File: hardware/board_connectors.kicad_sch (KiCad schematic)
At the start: 15 parts, among them J1 AudioJack2_Ground, J3 Conn_01x02, J5 AudioJack2_Ground, J6 Conn_02x03_Odd_Even, J7 AudioJack2_Ground, J7 USB_B_Micro

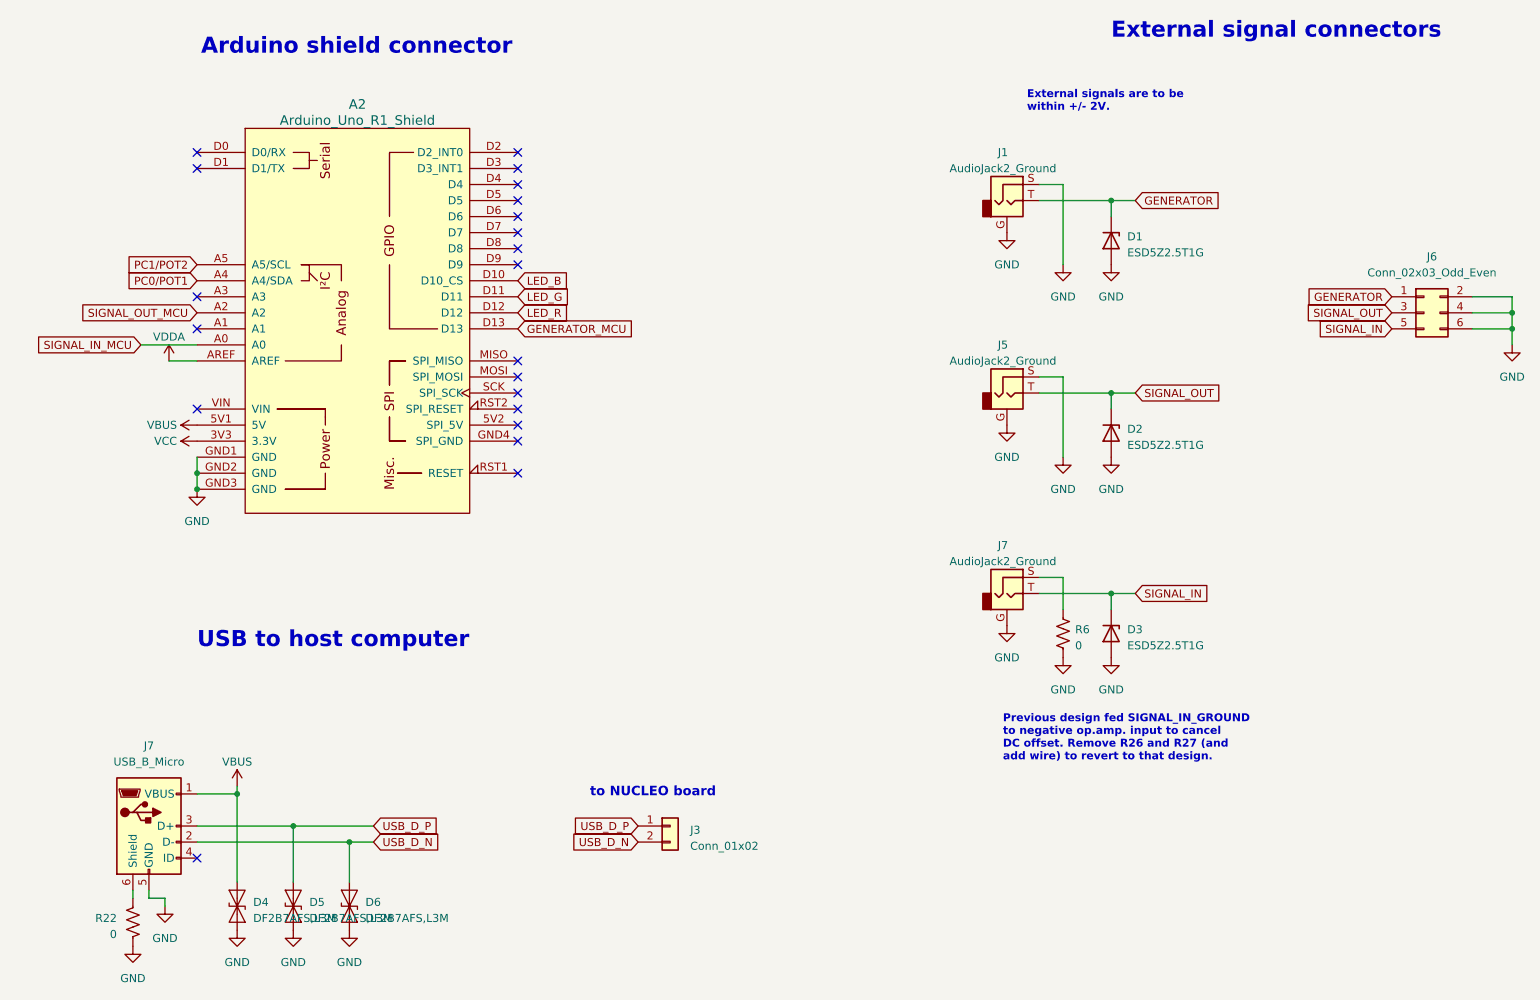
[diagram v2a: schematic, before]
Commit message: use nucleo 3.3v vdda; add 2nd low-pass stage to input
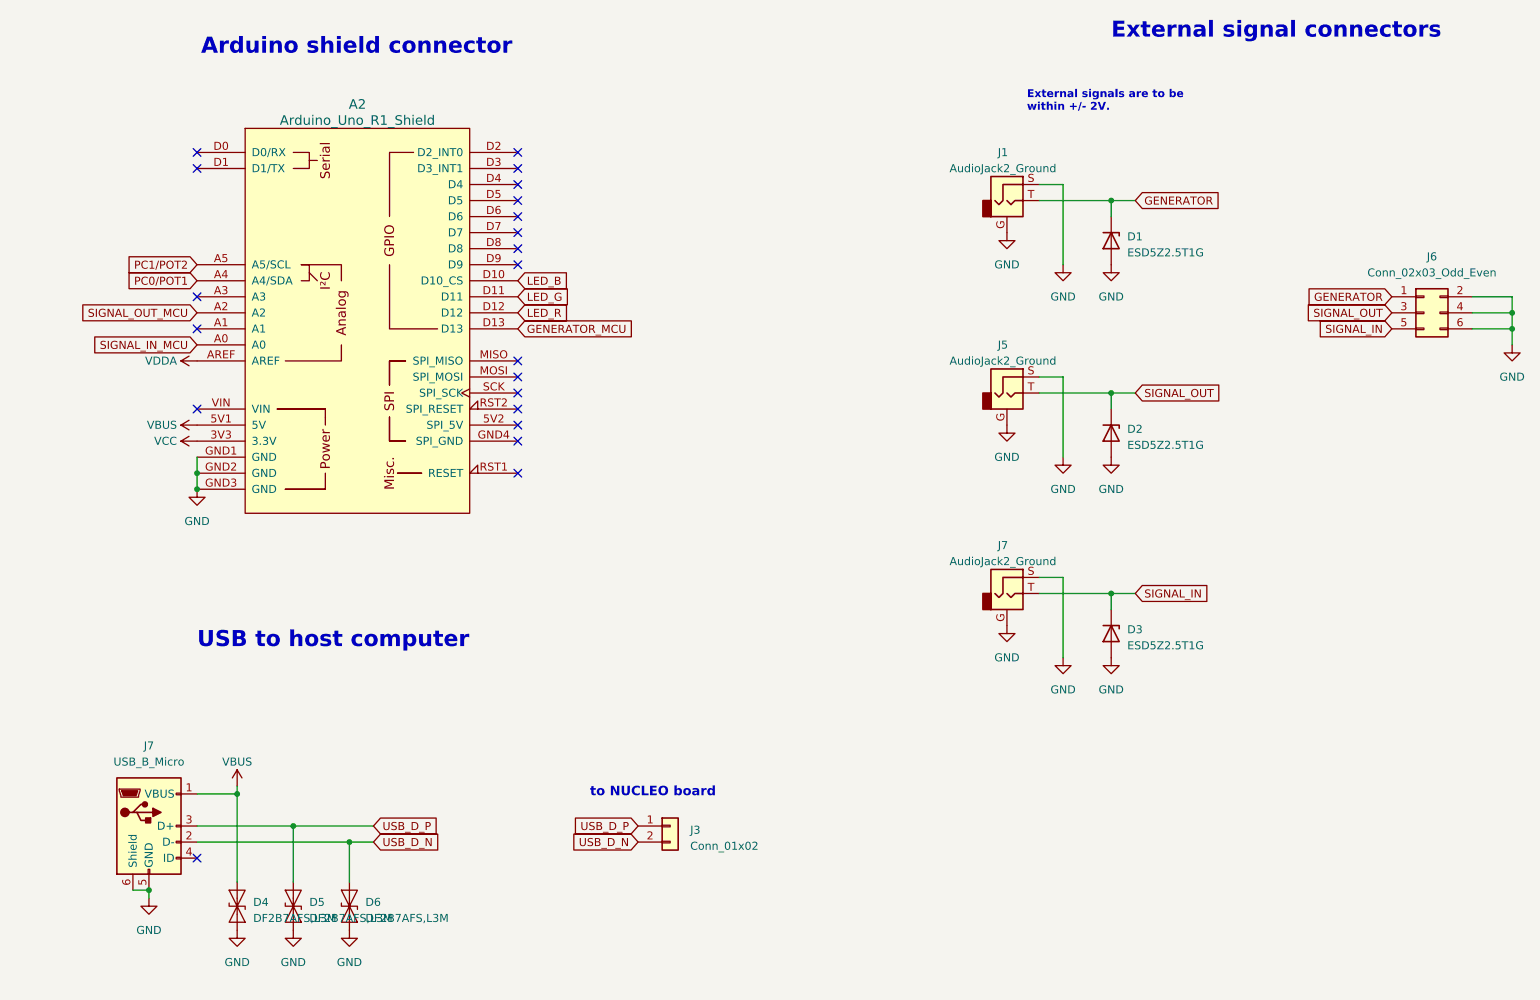
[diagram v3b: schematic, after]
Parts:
- removed R22, R6: 0, Resistor_SMD:R_0603_1608Metric, symbol Device:R_US
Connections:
- net GND: now also J7.6 (Shield), J7.S
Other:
- note removed: "Previous design fed SIGNAL_IN_GROUND to negative op.amp. input to cancel DC offset. Remove R26 and R27 (and add wire) to revert to that design."
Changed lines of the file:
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@@
   (title_block
     (title "DSP PAW add-on board")
-    (date "2023-09-04")
+    (date "2023-09-13")
     (rev "2")
     (company "bitgloo")
@@
   )
   (junction (at 257.81 72.39) (diameter 0) (color 0 0 0 0)
+  )
+  (junction (at 41.91 163.83) (diameter 0) (color 0 0 0 0)
   )
   (junction (at 49.53 97.79) (diameter 0) (color 0 0 0 0)
@@
     (stroke (width 0) (type default))
   )
-  (wire (pts (xy 186.69 114.3) (xy 186.69 119.38))
+  (wire (pts (xy 186.69 114.3) (xy 186.69 127))
     (stroke (width 0) (type default))
   )
@@
     (stroke (width 0) (type default))
   )
-  (wire (pts (xy 45.085 80.01) (xy 49.53 80.01))
-    (stroke (width 0) (type default))
-  )
   (wire (pts (xy 194.31 54.61) (xy 194.31 57.15))
     (stroke (width 0) (type default))
@@
     (stroke (width 0) (type default))
   )
+  (wire (pts (xy 39.37 163.83) (xy 41.91 163.83))
+    (stroke (width 0) (type default))
+  )
   (wire (pts (xy 194.31 85.09) (xy 194.31 87.63))
     (stroke (width 0) (type default))
@@
     (stroke (width 0) (type default))
   )
-  (wire (pts (xy 40.64 77.47) (xy 49.53 77.47))
-    (stroke (width 0) (type default))
-  )
-  (wire (pts (xy 44.45 165.1) (xy 41.91 165.1))
-    (stroke (width 0) (type default))
-  )
   (wire (pts (xy 182.88 52.07) (xy 186.69 52.07))
     (stroke (width 0) (type default))
@@
     (stroke (width 0) (type default))
   )
-  (wire (pts (xy 39.37 163.83) (xy 39.37 165.1))
-    (stroke (width 0) (type default))
-  )
   (wire (pts (xy 49.53 95.25) (xy 49.53 97.79))
     (stroke (width 0) (type default))
@@
     (stroke (width 0) (type default))
   )
-  (wire (pts (xy 44.45 166.37) (xy 44.45 165.1))
-    (stroke (width 0) (type default))
-  )
-  (wire (pts (xy 41.91 165.1) (xy 41.91 163.83))
-    (stroke (width 0) (type default))
-  )
   (wire (pts (xy 64.77 153.67) (xy 64.77 162.56))
+    (stroke (width 0) (type default))
+  )
+  (wire (pts (xy 41.91 163.83) (xy 41.91 165.1))
     (stroke (width 0) (type default))
   )
@@
   (text "External signal connectors" (at 194.31 29.21 0)
     (effects (font (size 2.54 2.54) (thickness 0.254) bold) (justify left bottom))
-  )
-  (text "Previous design fed SIGNAL_IN_GROUND\nto negative op.amp. input to cancel\nDC offset. Remove R26 and R27 (and\nadd wire) to revert to that design."
-    (at 177.165 143.51 0)
-    (effects (font (size 1.25 1.25) (thickness 0.254) bold) (justify left bottom))
   )
   (global_label "USB_D_P" (shape input) (at 119.38 153.67 180) (fields_autoplaced)
@@
     )
   )
-  (global_label "SIGNAL_IN_MCU" (shape input) (at 40.64 77.47 180) (fields_autoplaced)
+  (global_label "SIGNAL_IN_MCU" (shape input) (at 49.53 77.47 180) (fields_autoplaced)
     (effects (font (size 1.27 1.27)) (justify right))
-    (property "Intersheetrefs" "${INTERSHEET_REFS}" (at 23.2803 77.47 0)
+    (property "Intersheetrefs" "${INTERSHEET_REFS}" (at 32.1703 77.47 0)
       (effects (font (size 1.27 1.27)) (justify right) hide)
     )
@@
     )
   )
-  (symbol (lib_id "power:VDDA") (at 45.085 80.01 0) (unit 1)
+  (symbol (lib_id "power:VDDA") (at 49.53 80.01 90) (unit 1)
     (in_bom yes) (on_board yes) (dnp no)
-    (property "Reference" "#PWR04" (at 45.085 83.82 0)
-      (effects (font (size 1.27 1.27)) hide)
-    )
-    (property "Value" "VDDA" (at 45.085 76.2 0)
-      (effects (font (size 1.27 1.27)))
-    )
-    (property "Footprint" "" (at 45.085 80.01 0)
-      (effects (font (size 1.27 1.27)) hide)
-    )
-    (property "Datasheet" "" (at 45.085 80.01 0)
+    (property "Reference" "#PWR04" (at 53.34 80.01 0)
+      (effects (font (size 1.27 1.27)) hide)
+    )
+    (property "Value" "VDDA" (at 46.355 80.01 90)
+      (effects (font (size 1.27 1.27)) (justify left))
+    )
+    (property "Footprint" "" (at 49.53 80.01 0)
+      (effects (font (size 1.27 1.27)) hide)
+    )
+    (property "Datasheet" "" (at 49.53 80.01 0)
       (effects (font (size 1.27 1.27)) hide)
     )
@@
     )
   )
-  (symbol (lib_id "power:GND") (at 44.45 166.37 0) (unit 1)
-    (in_bom yes) (on_board yes) (dnp no) (fields_autoplaced)
-    (property "Reference" "#PWR038" (at 44.45 172.72 0)
-      (effects (font (size 1.27 1.27)) hide)
-    )
-    (property "Value" "GND" (at 44.45 171.45 0)
-      (effects (font (size 1.27 1.27)))
-    )
-    (property "Footprint" "" (at 44.45 166.37 0)
-      (effects (font (size 1.27 1.27)) hide)
-    )
-    (property "Datasheet" "" (at 44.45 166.37 0)
-      (effects (font (size 1.27 1.27)) hide)
-    )
-    (pin "1")
-    (instances
-      (project "stmdsp_rev3"
-        (path "/975c3983-57e7-4e06-a697-831e5209dd80"
-          (reference "#PWR038") (unit 1)
-        )
-      )
-      (project "DSP PAW add-on board"
-        (path "/c291319b-d76e-4fda-91cc-061acff65f9f/270d19d2-3af2-41db-ad1c-33373417ec82"
-          (reference "#PWR062") (unit 1)
-        )
-      )
-    )
-  )
   (symbol (lib_id "power:GND") (at 55.88 170.18 0) (unit 1)
     (in_bom yes) (on_board yes) (dnp no) (fields_autoplaced)
@@
     )
   )
-  (symbol (lib_id "Device:R_US") (at 186.69 123.19 180) (unit 1)
-    (in_bom yes) (on_board yes) (dnp no) (fields_autoplaced)
-    (property "Reference" "R6" (at 188.595 122.555 0)
-      (effects (font (size 1.27 1.27)) (justify right))
-    )
-    (property "Value" "0" (at 188.595 125.095 0)
-      (effects (font (size 1.27 1.27)) (justify right))
-    )
-    (property "Footprint" "Resistor_SMD:R_0603_1608Metric" (at 185.674 122.936 90)
-      (effects (font (size 1.27 1.27)) hide)
-    )
-    (property "Datasheet" "~" (at 186.69 123.19 0)
-      (effects (font (size 1.27 1.27)) hide)
-    )
-    (property "Part Number" "RMCF0603ZT0R00" (at 186.69 123.19 0)
-      (effects (font (size 1.27 1.27)) hide)
-    )
-    (property "DNP" "" (at 186.69 123.19 0)
-      (effects (font (size 1.27 1.27)) hide)
-    )
-    (pin "1")
-    (pin "2")
-    (instances
-      (project "DSP PAW add-on board"
-        (path "/c291319b-d76e-4fda-91cc-061acff65f9f/684072e7-f538-4528-bfb8-b14c31b5b1f0"
-          (reference "R6") (unit 1)
-        )
-        (path "/c291319b-d76e-4fda-91cc-061acff65f9f/270d19d2-3af2-41db-ad1c-33373417ec82"
-          (reference "R26") (unit 1)
-        )
-      )
-    )
-  )
   (symbol (lib_id "Connector_Audio:AudioJack2_Ground") (at 177.8 116.84 0) (unit 1)
     (in_bom yes) (on_board yes) (dnp no) (fields_autoplaced)
@@
         (path "/c291319b-d76e-4fda-91cc-061acff65f9f/270d19d2-3af2-41db-ad1c-33373417ec82"
           (reference "#PWR060") (unit 1)
-        )
-      )
-    )
-  )
-  (symbol (lib_id "Device:R_US") (at 39.37 168.91 0) (mirror y) (unit 1)
-    (in_bom yes) (on_board yes) (dnp no)
-    (property "Reference" "R22" (at 36.83 168.275 0)
-      (effects (font (size 1.27 1.27)) (justify left))
-    )
-    (property "Value" "0" (at 36.83 170.815 0)
-      (effects (font (size 1.27 1.27)) (justify left))
-    )
-    (property "Footprint" "Resistor_SMD:R_0603_1608Metric" (at 38.354 169.164 90)
-      (effects (font (size 1.27 1.27)) hide)
-    )
-    (property "Datasheet" "~" (at 39.37 168.91 0)
-      (effects (font (size 1.27 1.27)) hide)
-    )
-    (property "Part Number" "RMCF0603ZT0R00" (at 39.37 168.91 0)
-      (effects (font (size 1.27 1.27)) hide)
-    )
-    (property "DNP" "" (at 39.37 168.91 0)
-      (effects (font (size 1.27 1.27)) hide)
-    )
-    (pin "1")
-    (pin "2")
-    (instances
-      (project "DSP PAW add-on board"
-        (path "/c291319b-d76e-4fda-91cc-061acff65f9f/270d19d2-3af2-41db-ad1c-33373417ec82"
-          (reference "R22") (unit 1)
         )
       )
@@
     )
   )
-  (symbol (lib_id "power:GND") (at 39.37 172.72 0) (unit 1)
-    (in_bom yes) (on_board yes) (dnp no) (fields_autoplaced)
-    (property "Reference" "#PWR038" (at 39.37 179.07 0)
-      (effects (font (size 1.27 1.27)) hide)
-    )
-    (property "Value" "GND" (at 39.37 177.8 0)
-      (effects (font (size 1.27 1.27)))
-    )
-    (property "Footprint" "" (at 39.37 172.72 0)
-      (effects (font (size 1.27 1.27)) hide)
-    )
-    (property "Datasheet" "" (at 39.37 172.72 0)
-      (effects (font (size 1.27 1.27)) hide)
-    )
+  (symbol (lib_id "power:GND") (at 41.91 165.1 0) (unit 1)
+    (in_bom yes) (on_board yes) (dnp no) (fields_autoplaced)
+    (property "Reference" "#PWR038" (at 41.91 171.45 0)
+      (effects (font (size 1.27 1.27)) hide)
+    )
+    (property "Value" "GND" (at 41.91 170.18 0)
+      (effects (font (size 1.27 1.27)))
+    )
+    (property "Footprint" "" (at 41.91 165.1 0)
+      (effects (font (size 1.27 1.27)) hide)
+    )
+    (property "Datasheet" "" (at 41.91 165.1 0)
+      (effects (font (size 1.27 1.27)) hide)
+    )

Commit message: finalize rev2 schematic
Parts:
- J1, J5, J7: Part Number 2 -> SJ-3523-SMT-TR
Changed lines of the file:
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@@
       (effects (font (size 1.27 1.27)) hide)
     )
-    (property "Part Number" "2" (at 177.8 85.09 0)
+    (property "Part Number" "SJ-3523-SMT-TR" (at 177.8 85.09 0)
       (effects (font (size 1.27 1.27)) hide)
     )
@@
       (effects (font (size 1.27 1.27)) hide)
     )
-    (property "Part Number" "2" (at 177.8 54.61 0)
+    (property "Part Number" "SJ-3523-SMT-TR" (at 177.8 54.61 0)
       (effects (font (size 1.27 1.27)) hide)
     )
@@
       (effects (font (size 1.27 1.27)) hide)
     )
-    (property "Part Number" "2" (at 177.8 116.84 0)
-      (effects (font (size 1.27 1.27)) hide)
-    )
+    (property "Part Number" "SJ-3523-SMT-TR" (at 177.8 116.84 0)
+      (effects (font (size 1.27 1.27)) hide)
+    )

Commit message: finish rev2 layout
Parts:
- J1, J5, J7: footprint Connector_Audio:Jack_3.5mm_CUI_SJ-3523-SMT_Horizontal -> Connector_Audio:Jack_3.5mm_PJ320D_Horizontal; symbol Connector_Audio:AudioJack2_Ground -> Connector_Audio:AudioJack4; Part Number SJ-3523-SMT-TR -> PJ-320D
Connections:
- net GND: no longer J1.G, J5.G, J7.G
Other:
- moved on the sheet: D1, D2, D3
